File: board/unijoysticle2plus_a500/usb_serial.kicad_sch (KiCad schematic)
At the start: 12 parts, among them J3 USB_B_Micro, U5 AMS1117-3.3, U6 CH340C

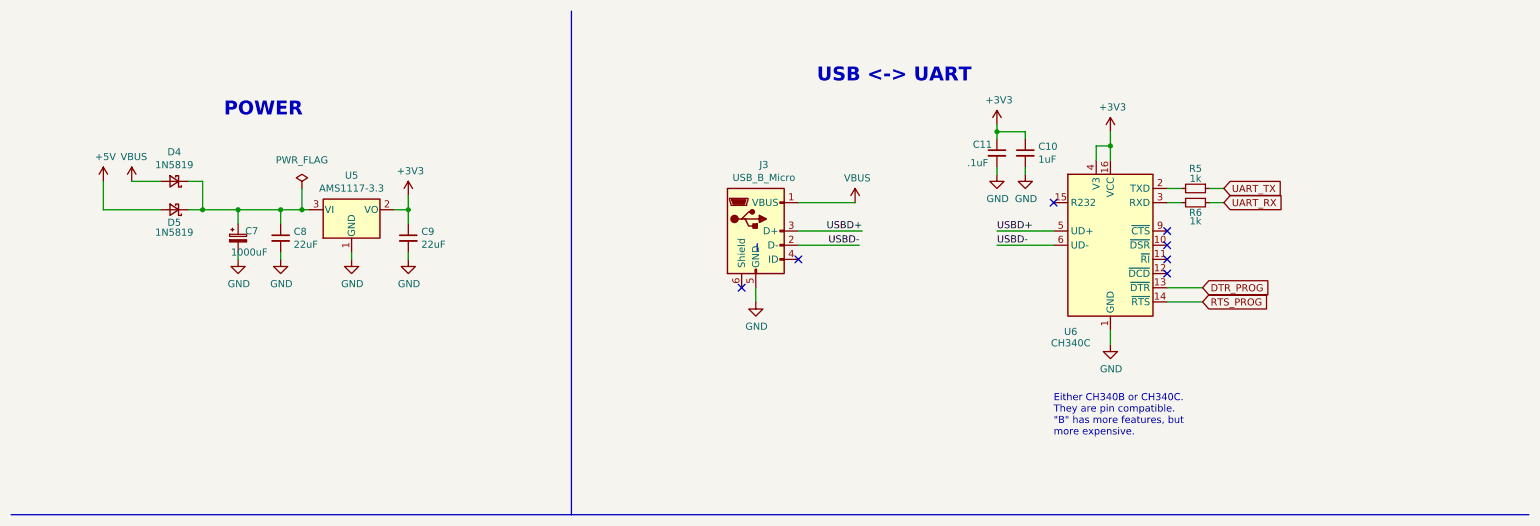
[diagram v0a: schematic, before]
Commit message: a500: remove duplicate symbols
It is able to run the EDR checks with 5 warnings.
Only one looks worth taking a look at.
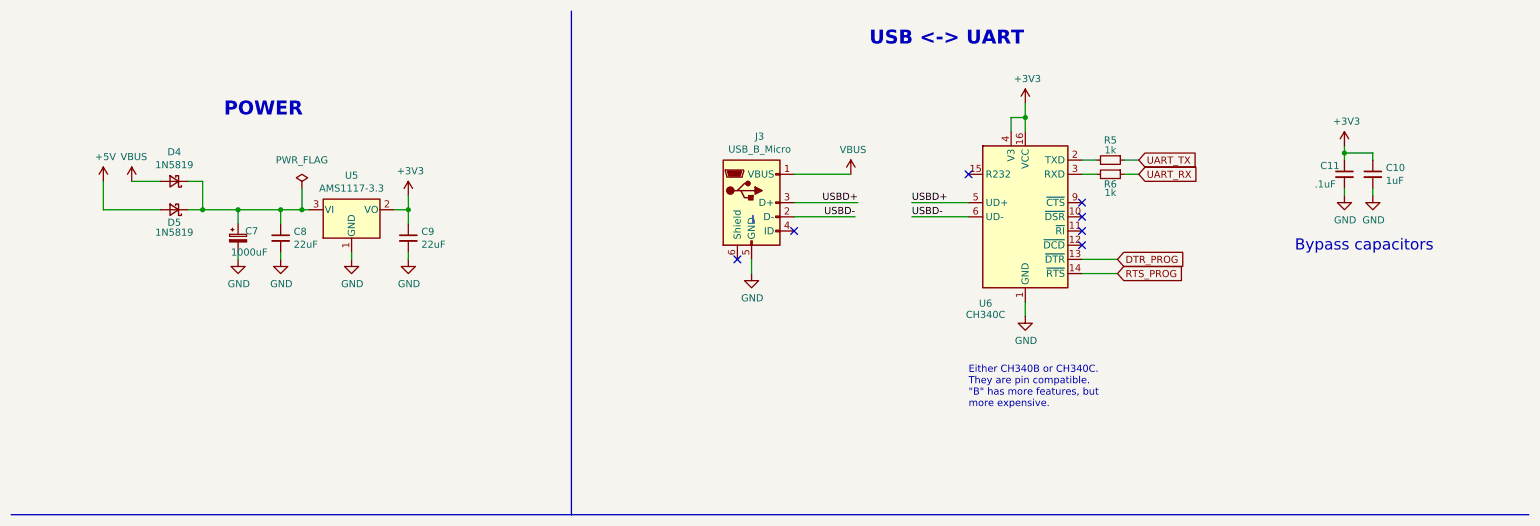
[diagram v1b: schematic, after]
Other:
- note added: "Bypass capacitors"
- moved on the sheet: C10, C11, J3, R5, R6, U6

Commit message: uni2+ a500: schematic "ready"
The schematic should be "ready".
Layout WIP. Components were placed in "place".
But routing is missing, as well as logos
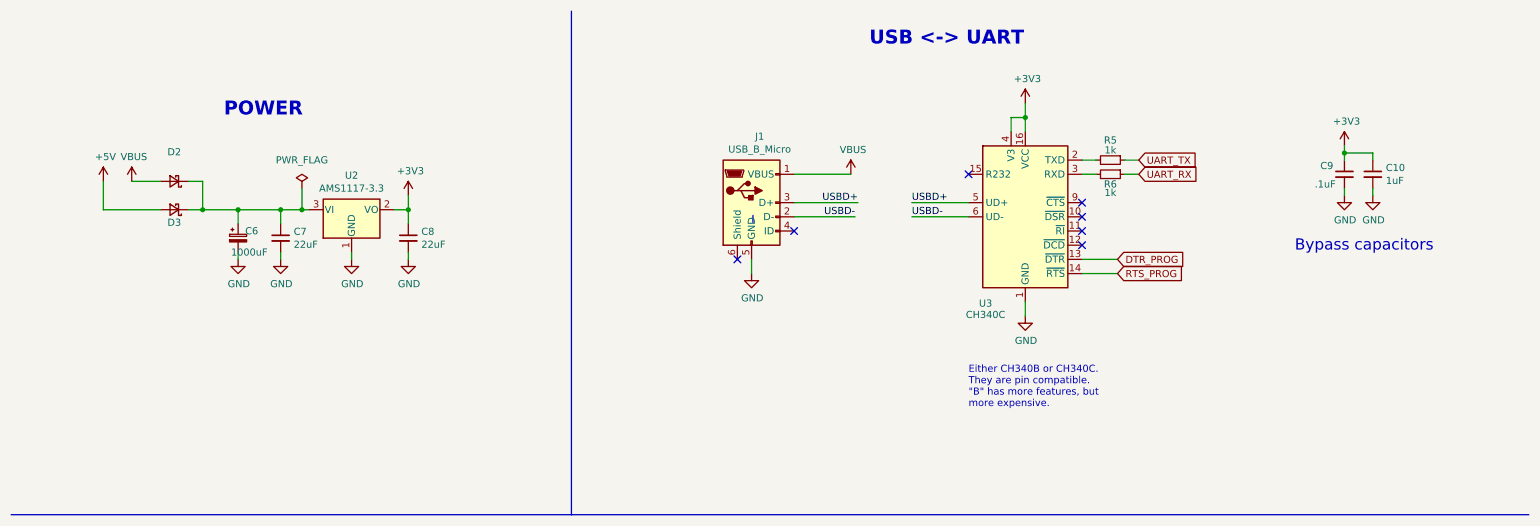
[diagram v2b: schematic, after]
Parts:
- D2: renamed from D4; value 1N5819 -> (none); footprint Diode_SMD:D_SOD-123 -> (none)
- D3: renamed from D5; value 1N5819 -> (none); footprint Diode_SMD:D_SOD-123 -> (none)
- renumbered C7 to C6, C8 to C7, C9 to C8, C11 to C9, J3 to J1, U5 to U2, U6 to U3
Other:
- title: Unijoysticle 2+ -> Unijoysticle 2+ A500
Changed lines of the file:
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@@
   (paper "A4")
   (title_block
-    (title "Unijoysticle 2+")
-    (date "2022-01-02")
-    (rev "H")
+    (title "Unijoysticle 2+ A500")
+    (date "2022-04-20")
+    (rev "A")
     (company "Retro Moe")
   )
@@
   (symbol (lib_id "power:VBUS") (at 163.068 41.91 0) (unit 1)
     (in_bom yes) (on_board yes)
-    (property "Reference" "#PWR025" (id 0) (at 163.068 45.72 0)
+    (property "Reference" "#PWR019" (id 0) (at 163.068 45.72 0)
       (effects (font (size 1.27 1.27)) hide)
     )
@@
   (symbol (lib_id "Device:C_Small") (at 60.96 53.34 0) (unit 1)
     (in_bom yes) (on_board yes)
-    (property "Reference" "C8" (id 0) (at 63.2968 52.1716 0)
+    (property "Reference" "C7" (id 0) (at 63.2968 52.1716 0)
       (effects (font (size 1.27 1.27)) (justify left))
     )
@@
   (symbol (lib_id "power:GND") (at 73.66 57.15 0) (unit 1)
     (in_bom yes) (on_board yes)
-    (property "Reference" "#PWR026" (id 0) (at 73.66 63.5 0)
+    (property "Reference" "#PWR015" (id 0) (at 73.66 63.5 0)
       (effects (font (size 1.27 1.27)) hide)
     )
@@
   (symbol (lib_id "power:GND") (at 60.96 57.15 0) (unit 1)
     (in_bom yes) (on_board yes)
-    (property "Reference" "#PWR024" (id 0) (at 60.96 63.5 0)
+    (property "Reference" "#PWR014" (id 0) (at 60.96 63.5 0)
       (effects (font (size 1.27 1.27)) hide)
     )
@@
   (symbol (lib_id "Device:C_Small") (at 83.82 53.34 0) (unit 1)
     (in_bom yes) (on_board yes)
-    (property "Reference" "C9" (id 0) (at 86.1568 52.1716 0)
+    (property "Reference" "C8" (id 0) (at 86.1568 52.1716 0)
       (effects (font (size 1.27 1.27)) (justify left))
     )
@@
   (symbol (lib_id "power:GND") (at 83.82 57.15 0) (unit 1)
     (in_bom yes) (on_board yes)
-    (property "Reference" "#PWR029" (id 0) (at 83.82 63.5 0)
+    (property "Reference" "#PWR017" (id 0) (at 83.82 63.5 0)
       (effects (font (size 1.27 1.27)) hide)
     )
@@
   (symbol (lib_id "power:+3V3") (at 83.82 45.72 0) (unit 1)
     (in_bom yes) (on_board yes)
-    (property "Reference" "#PWR028" (id 0) (at 83.82 49.53 0)
+    (property "Reference" "#PWR016" (id 0) (at 83.82 49.53 0)
       (effects (font (size 1.27 1.27)) hide)
     )
@@
   (symbol (lib_id "Regulator_Linear:AMS1117-3.3") (at 73.66 48.26 0) (unit 1)
     (in_bom yes) (on_board yes)
-    (property "Reference" "U5" (id 0) (at 73.66 42.1132 0))
+    (property "Reference" "U2" (id 0) (at 73.66 42.1132 0))
     (property "Value" "AMS1117-3.3" (id 1) (at 73.66 44.4246 0))
     (property "Footprint" "Package_TO_SOT_SMD:SOT-223-3_TabPin2" (id 2) (at 73.66 43.18 0)
@@
   (symbol (lib_id "Interface_USB:CH340C") (at 194.31 49.53 0) (unit 1)
     (in_bom yes) (on_board yes)
-    (property "Reference" "U6" (id 0) (at 187.198 65.024 0))
+    (property "Reference" "U3" (id 0) (at 187.198 65.024 0))
     (property "Value" "CH340C" (id 1) (at 187.198 67.056 0))
     (property "Footprint" "Package_SO:SOIC-16_3.9x9.9mm_P1.27mm" (id 2) (at 195.58 63.5 0)
@@
   (symbol (lib_id "power:GND") (at 251.46 45.72 0) (unit 1)
     (in_bom yes) (on_board yes)
-    (property "Reference" "#PWR0103" (id 0) (at 251.46 52.07 0)
+    (property "Reference" "#PWR023" (id 0) (at 251.46 52.07 0)
       (effects (font (size 1.27 1.27)) hide)
     )
@@
   (symbol (lib_id "Device:C_Small") (at 251.46 41.91 0) (unit 1)
     (in_bom yes) (on_board yes)
-    (property "Reference" "C11" (id 0) (at 247.142 40.386 0)
+    (property "Reference" "C9" (id 0) (at 247.142 40.386 0)
       (effects (font (size 1.27 1.27)) (justify left))
     )
@@
   (symbol (lib_id "power:VBUS") (at 34.29 43.18 0) (unit 1)
     (in_bom yes) (on_board yes)
-    (property "Reference" "#PWR022" (id 0) (at 34.29 46.99 0)
+    (property "Reference" "#PWR012" (id 0) (at 34.29 46.99 0)
       (effects (font (size 1.27 1.27)) hide)
     )
@@
   (symbol (lib_id "power:GND") (at 53.34 57.15 0) (unit 1)
     (in_bom yes) (on_board yes)
-    (property "Reference" "#PWR018" (id 0) (at 53.34 63.5 0)
+    (property "Reference" "#PWR013" (id 0) (at 53.34 63.5 0)
       (effects (font (size 1.27 1.27)) hide)
     )
@@
   (symbol (lib_id "power:+3V3") (at 194.31 29.21 0) (unit 1)
     (in_bom yes) (on_board yes)
-    (property "Reference" "#PWR0101" (id 0) (at 194.31 33.02 0)
+    (property "Reference" "#PWR020" (id 0) (at 194.31 33.02 0)
       (effects (font (size 1.27 1.27)) hide)
     )
@@
   (symbol (lib_id "power:GND") (at 194.31 67.31 0) (unit 1)
     (in_bom yes) (on_board yes)
-    (property "Reference" "#PWR0102" (id 0) (at 194.31 73.66 0)
+    (property "Reference" "#PWR021" (id 0) (at 194.31 73.66 0)
       (effects (font (size 1.27 1.27)) hide)
     )
@@
   (symbol (lib_id "power:+3V3") (at 251.46 36.83 0) (unit 1)
     (in_bom yes) (on_board yes)
-    (property "Reference" "#PWR0105" (id 0) (at 251.46 40.64 0)
+    (property "Reference" "#PWR022" (id 0) (at 251.46 40.64 0)
       (effects (font (size 1.27 1.27)) hide)
     )
@@
   (symbol (lib_id "power:GND") (at 256.54 45.72 0) (unit 1)
     (in_bom yes) (on_board yes)
-    (property "Reference" "#PWR0106" (id 0) (at 256.54 52.07 0)
+    (property "Reference" "#PWR024" (id 0) (at 256.54 52.07 0)
       (effects (font (size 1.27 1.27)) hide)
     )
@@
   (symbol (lib_id "power:GND") (at 145.288 59.69 0) (unit 1)
     (in_bom yes) (on_board yes)
-    (property "Reference" "#PWR0107" (id 0) (at 145.288 66.04 0)
+    (property "Reference" "#PWR018" (id 0) (at 145.288 66.04 0)
       (effects (font (size 1.27 1.27)) hide)
     )
@@
   (symbol (lib_id "Device:D_Schottky_Small") (at 41.91 43.18 180) (unit 1)
     (in_bom yes) (on_board yes)
-    (property "Reference" "D4" (id 0) (at 41.91 37.9222 0))
-    (property "Value" "1N5819" (id 1) (at 41.91 40.2336 0))
-    (property "Footprint" "Diode_SMD:D_SOD-123" (id 2) (at 41.91 43.18 90)
+    (property "Reference" "D2" (id 0) (at 41.91 37.9222 0))
+    (property "Value" "" (id 1) (at 41.91 40.2336 0))
+    (property "Footprint" "" (id 2) (at 41.91 43.18 90)
       (effects (font (size 1.27 1.27)) hide)
     )
@@
   (symbol (lib_id "Device:D_Schottky_Small") (at 41.91 48.26 180) (unit 1)
     (in_bom yes) (on_board yes)
-    (property "Reference" "D5" (id 0) (at 41.91 50.546 0))
-    (property "Value" "1N5819" (id 1) (at 41.91 52.324 0))
-    (property "Footprint" "Diode_SMD:D_SOD-123" (id 2) (at 41.91 48.26 90)
+    (property "Reference" "D3" (id 0) (at 41.91 50.546 0))
+    (property "Value" "" (id 1) (at 41.91 52.324 0))
+    (property "Footprint" "" (id 2) (at 41.91 48.26 90)
       (effects (font (size 1.27 1.27)) hide)
     )
@@
   (symbol (lib_id "Connector:USB_B_Micro") (at 145.288 46.99 0) (unit 1)
     (in_bom yes) (on_board yes)
-    (property "Reference" "J3" (id 0) (at 146.7358 35.1282 0))
+    (property "Reference" "J1" (id 0) (at 146.7358 35.1282 0))
     (property "Value" "USB_B_Micro" (id 1) (at 146.7358 37.4396 0))
     (property "Footprint" "Connector_USB:USB_Micro-B_Amphenol_10118194_Horizontal" (id 2) (at 149.098 48.26 0)
@@
   (symbol (lib_id "power:+5V") (at 29.21 43.18 0) (unit 1)
     (in_bom yes) (on_board yes)
-    (property "Reference" "#PWR0109" (id 0) (at 29.21 46.99 0)
+    (property "Reference" "#PWR011" (id 0) (at 29.21 46.99 0)
       (effects (font (size 1.27 1.27)) hide)
     )
@@
   (symbol (lib_id "power:PWR_FLAG") (at 64.77 44.45 0) (unit 1)
     (in_bom yes) (on_board yes) (fields_autoplaced)
-    (property "Reference" "#FLG0101" (id 0) (at 64.77 42.545 0)
+    (property "Reference" "#FLG01" (id 0) (at 64.77 42.545 0)
       (effects (font (size 1.27 1.27)) hide)
     )
@@
   (symbol (lib_id "Device:C_Polarized_Small") (at 53.34 53.34 0) (unit 1)
     (in_bom yes) (on_board yes)
-    (property "Reference" "C7" (id 0) (at 54.61 52.07 0)
-      (effects (font (size 1.27 1.27)) (justify left))
-    )
+    (property "Reference" "C6" (id 0) (at 54.61 52.07 0)
+      (effects (font (size 1.27 1.27)) (justify left))
+    )

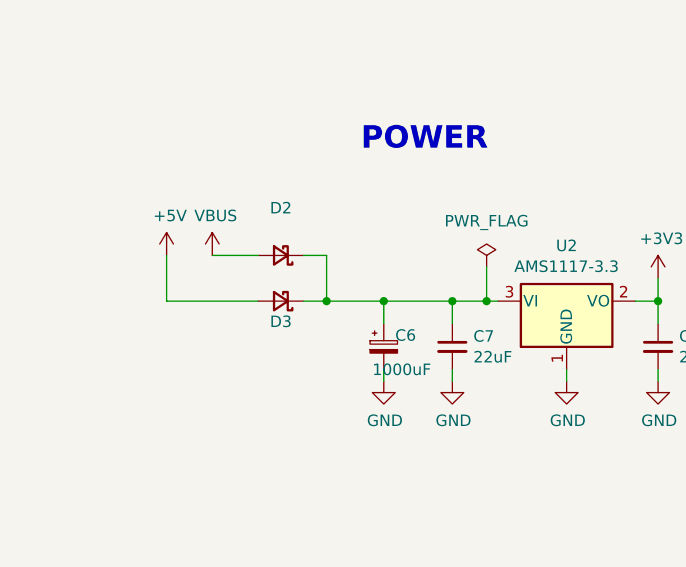
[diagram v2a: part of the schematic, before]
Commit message: uni a500: manual routing
WIP... all wires connected. requires to double check everything
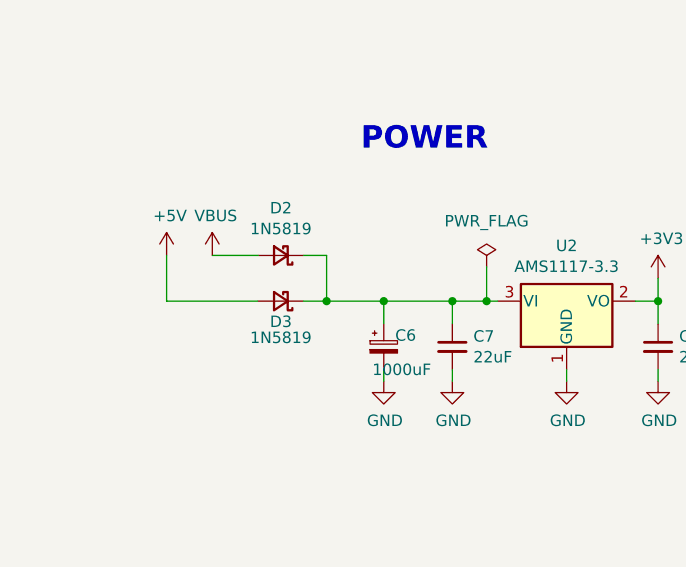
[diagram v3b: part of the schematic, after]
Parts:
- D2, D3: value (none) -> 1N5819; footprint (none) -> Diode_SMD:D_SOD-123
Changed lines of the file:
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@@
     (in_bom yes) (on_board yes)
     (property "Reference" "D2" (id 0) (at 41.91 37.9222 0))
-    (property "Value" "" (id 1) (at 41.91 40.2336 0))
-    (property "Footprint" "" (id 2) (at 41.91 43.18 90)
+    (property "Value" "1N5819" (id 1) (at 41.91 40.2336 0))
+    (property "Footprint" "Diode_SMD:D_SOD-123" (id 2) (at 41.91 43.18 90)
       (effects (font (size 1.27 1.27)) hide)
     )
@@
     (in_bom yes) (on_board yes)
     (property "Reference" "D3" (id 0) (at 41.91 50.546 0))
-    (property "Value" "" (id 1) (at 41.91 52.324 0))
-    (property "Footprint" "" (id 2) (at 41.91 48.26 90)
+    (property "Value" "1N5819" (id 1) (at 41.91 52.324 0))
+    (property "Footprint" "Diode_SMD:D_SOD-123" (id 2) (at 41.91 48.26 90)
       (effects (font (size 1.27 1.27)) hide)
     )

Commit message: Rename Uni2+ A500 to Uni2 A500
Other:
- title: Unijoysticle 2+ A500 -> Unijoysticle 2 A500
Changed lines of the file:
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@@
   (paper "A4")
   (title_block
-    (title "Unijoysticle 2+ A500")
-    (date "2022-04-20")
+    (title "Unijoysticle 2 A500")
+    (date "2022-04-25")
     (rev "A")
     (company "Retro Moe")
